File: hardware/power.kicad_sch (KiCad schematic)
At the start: 87 parts, among them J3 Vcore_sel, U1 TLV62569DBV, U2 TLV62569DBV, U3 MPM3833CGRH-Z, U4 GateMate-CCGM1A1, U5 TLV62569DBV

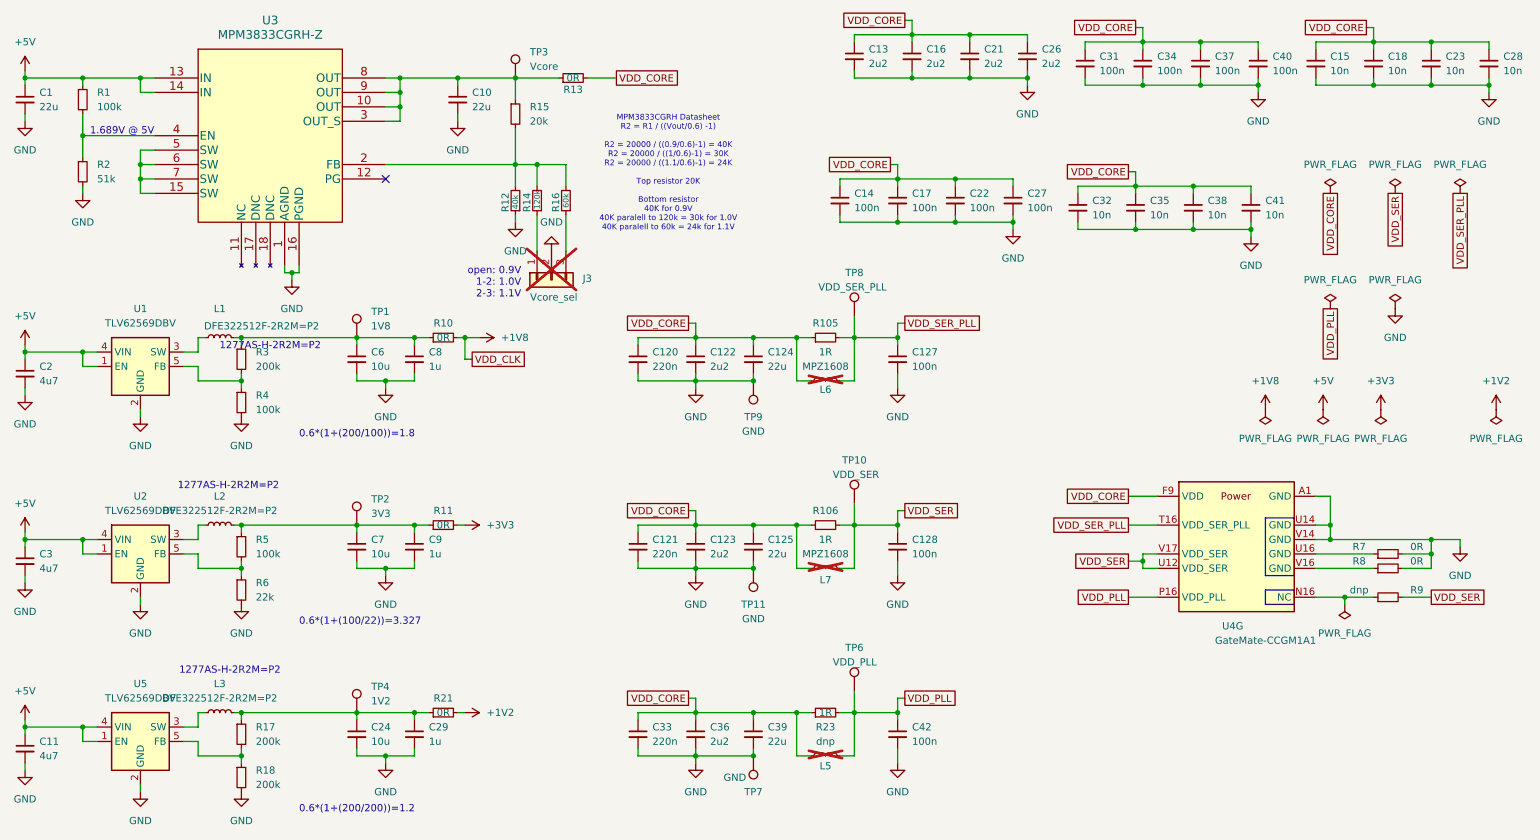
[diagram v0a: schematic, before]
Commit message: Improve SerDes routing, tunning ETH pairs, moving parts - fix #31
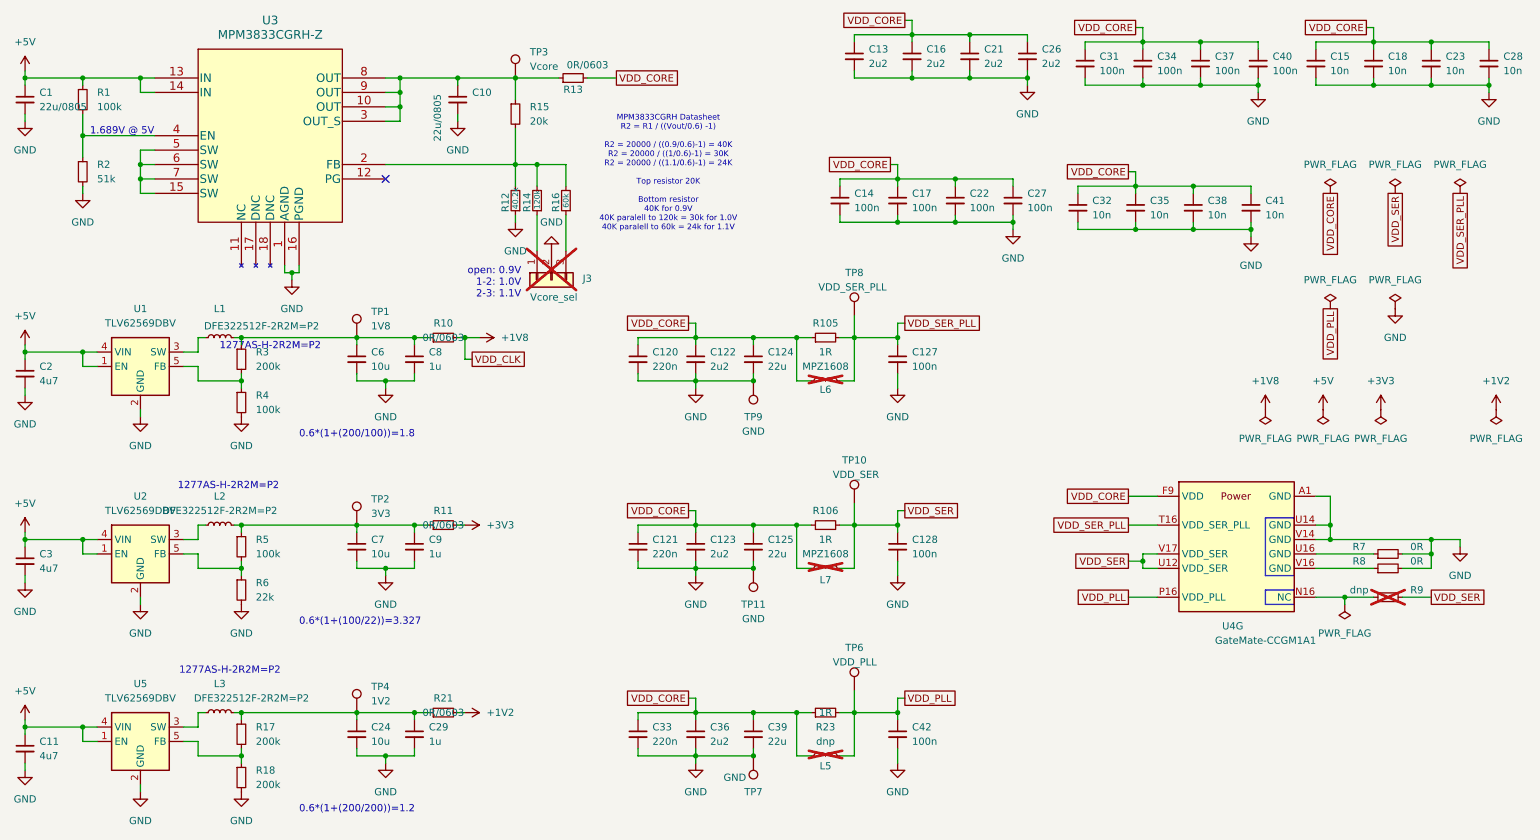
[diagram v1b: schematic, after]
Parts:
- C1, C10: value 22u -> 22u/0805; LCSC (none) -> C318688; MPN (none) -> CL21A226KPCLRNC; Mouser (none) -> https://hr.mouser.com/ProductDetail/Samsung-Electro-Mechani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; Mouser Part Number (none) -> 187-CL21A226KPCLRNC
- C11, C2, C3: LCSC (none) -> C469468; MPN (none) -> CC0402MRX5R6BB475; Mouser (none) -> https://hr.mouser.com/ProductDetail/YAGEO/CC0402MRX5R6BB475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; Mouser Part Number (none) -> 603-CC402MRX5R6BB475
- C120, C121, C33: LCSC (none) -> C16772; MPN (none) -> CL05B224KO5NNNC; Mouser (none) -> https://hr.mouser.com/ProductDetail/Samsung-Electro-Mechani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; Mouser Part Number (none) -> 187-CL05B224KO5NNNC
- C122, C123, C13, C16, C21, C26, C36: LCSC (none) -> C12530; MPN (none) -> CL05A225MQ5NSNC; Mouser (none) -> https://hr.mouser.com/ProductDetail/Samsung-Electro-Mechani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; Mouser Part Number (none) -> 187-CL05A225MQ5NSNC
- C124, C125, C39: LCSC (none) -> C15525; MPN (none) -> CL05A226MQ5N6J8; Mouser (none) -> https://hr.mouser.com/ProductDetail/Samsung-Electro-Mechani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; Mouser Part Number (none) -> 187-CL05A226MQ5N6J8
- C127, C128, C14, C17, C22, C27, C31, C34, C37, C40, C42: LCSC (none) -> C1525; MPN (none) -> GRM155R60J104KA01D; Mouser (none) -> https://hr.mouser.com/ProductDetail/Murata-Electronics/GRM1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; Mouser Part Number (none) -> 81-GRM155R60J104KA1D
- C15, C18, C23, C28, C32, C35, C38, C41: LCSC (none) -> C15195; MPN (none) -> CL05B103KB5NNNC; Mouser (none) -> https://hr.mouser.com/ProductDetail/Samsung-Electro-Mechani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; Mouser Part Number (none) -> 187-CL05B103KB5NNNC
- C24, C6, C7: LCSC (none) -> C15525; MPN (none) -> CL05A106MQ5NUNC; Mouser (none) -> https://hr.mouser.com/ProductDetail/Samsung-Electro-Mechani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; Mouser Part Number (none) -> 187-CL05A106MQ5NUNC
- C29, C8, C9: LCSC (none) -> C52923; MPN (none) -> CL05A105KA5NQNC; Mouser (none) -> https://hr.mouser.com/ProductDetail/Samsung-Electro-Mechani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; Mouser Part Number (none) -> 187-CL05A105KA5NQNC
- L1, L2, L3: LCSC (none) -> C3222669; MPN (none) -> DFE322512F-2R2M=P2; Mouser https://hr.mouser.com/ProductDetail/Murata-Electronics/1277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 -> https://hr.mouser.com/ProductDetail/Murata-Electronics/DFE3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; Mouser Part Number (none) -> 81-DFE322512F-2R2MP2
- R1, R4, R5: LCSC (none) -> C60491; MPN (none) -> RC0402FR-07100KL; Mouser (none) -> https://hr.mouser.com/ProductDetail/YAGEO/RC0402FR-07100KL?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; Mouser Part Number (none) -> 603-RC0402FR-07100KL
- R10, R11, R13, R21: value 0R -> 0R/0603; LCSC (none) -> C21189; MPN (none) -> AC0402FR-070RL; Mouser (none) -> https://hr.mouser.com/ProductDetail/YAGEO/AC0402FR-070RL?qs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; Mouser Part Number (none) -> 603-AC0402FR-070RL
- R105, R106, R23: LCSC (none) -> C144684; MPN (none) -> AC0603FR-071RL; Mouser (none) -> https://hr.mouser.com/ProductDetail/YAGEO/AC0603FR-071RL?qs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; Mouser Part Number (none) -> 603-AC0603FR-071RL
- R12: value 40k -> 40.2k; LCSC (none) -> C137983; MPN (none) -> RC0402FR-0740K2L; Mouser (none) -> https://hr.mouser.com/ProductDetail/YAGEO/RC0402FR-0740K2L?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; Mouser Part Number (none) -> 603-RC0402FR-0740K2L
- R14: LCSC (none) -> C144802; MPN (none) -> AC0402FR-07120KL; Mouser (none) -> https://hr.mouser.com/ProductDetail/YAGEO/AC0402FR-07120KL?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; Mouser Part Number (none) -> 603-AC0402FR-07120KL
- R15: LCSC (none) -> C144783; MPN (none) -> AC0402FR-0720KL; Mouser (none) -> https://hr.mouser.com/ProductDetail/YAGEO/AC0402FR-0720KL?q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; Mouser Part Number (none) -> 603-AC0402FR-0720KL
- R16: LCSC (none) -> C327333; MPN (none) -> RC0402FR-0760K4L; Mouser (none) -> https://hr.mouser.com/ProductDetail/YAGEO/RC0402FR-0760K4L?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; Mouser Part Number (none) -> 603-RC0402FR-0760K4L
- R17, R18, R3: LCSC (none) -> C114763; MPN (none) -> RC0402FR-07200KL; Mouser (none) -> https://hr.mouser.com/ProductDetail/YAGEO/AC0402FR-0751KL?q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; Mouser Part Number (none) -> 603-AC0402FR-0751KL
- R2: LCSC (none) -> C144749; MPN (none) -> AC0402FR-0751KL; Mouser (none) -> https://hr.mouser.com/ProductDetail/YAGEO/AC0402FR-0751KL?q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; Mouser Part Number (none) -> 603-AC0402FR-0751KL
- R6: LCSC (none) -> C482105; MPN (none) -> CRCW040222K0FKED; Mouser (none) -> https://hr.mouser.com/ProductDetail/Vishay/CRCW040222K0FKED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; Mouser Part Number (none) -> 71-CRCW0402-22K-E3
- R7, R8: LCSC (none) -> C226739; MPN (none) -> AC0402FR-070RL; Mouser (none) -> https://hr.mouser.com/ProductDetail/YAGEO/AC0402FR-070RL?qs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; Mouser Part Number (none) -> 603-AC0402FR-070RL
- R9: now not fitted; now left out of the parts list
- U1, U2, U5: LCSC (none) -> C141836; MPN (none) -> TLV62569DBVR; Mouser (none) -> https://hr.mouser.com/ProductDetail/Texas-Instruments/TLV62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; Mouser Part Number (none) -> 595-TLV62569DBVR
- U3: LCSC (none) -> C6306422; MPN (none) -> MPM3833CGRH-Z; Mouser (none) -> https://hr.mouser.com/ProductDetail/Monolithic-Power-System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; Mouser Part Number (none) -> 946-MPM3833CGRH-Z
- U4: LCSC (none) -> CCGM1A1-BGA324; MPN (none) -> CCGM1A1-BGA324

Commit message: v0.5 update
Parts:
- C124, C125, C39: LCSC C15525 -> C7423886
- L1, L2, L3: value DFE322512F-2R2M=P2 -> DFE252012F-2R2M=P2; LCSC C3222669 -> C576403; MPN DFE322512F-2R2M=P2 -> DFE252012F-2R2M=P2; Mouser https://hr.mouser.com/ProductDetail/Murata-Electronics/DFE3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 -> https://hr.mouser.com/en/ProductDetail/Murata-Electronics/D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; Mouser Part Number 81-DFE322512F-2R2MP2 -> 81-DFE252012F-2R2MP2
- R10, R11, R13, R21: MPN AC0402FR-070RL -> RC0603FR-070RL; Mouser https://hr.mouser.com/ProductDetail/YAGEO/AC0402FR-070RL?qs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 -> https://eu.mouser.com/en/ProductDetail/YAGEO/RC0603FR-070RL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; Mouser Part Number 603-AC0402FR-070RL -> 603-RC0603FR-070RL
- R17, R18, R3: Mouser https://hr.mouser.com/ProductDetail/YAGEO/AC0402FR-0751KL?q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 -> https://eu.mouser.com/en/ProductDetail/YAGEO/RC0402FR-07200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; Mouser Part Number 603-AC0402FR-0751KL -> 603-RC0402FR-07200KL
